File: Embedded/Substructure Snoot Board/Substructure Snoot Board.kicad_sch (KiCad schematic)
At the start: 33 parts, among them J1 10171746-00021LF, J2 PWR Jumper Pins, J3 L0 JST, J4 L1 JST, J6 A JST, J7 S Pins A, J8 S Pins B, U1 D0 FFC, U2 D1 FFC, U3 U FFC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

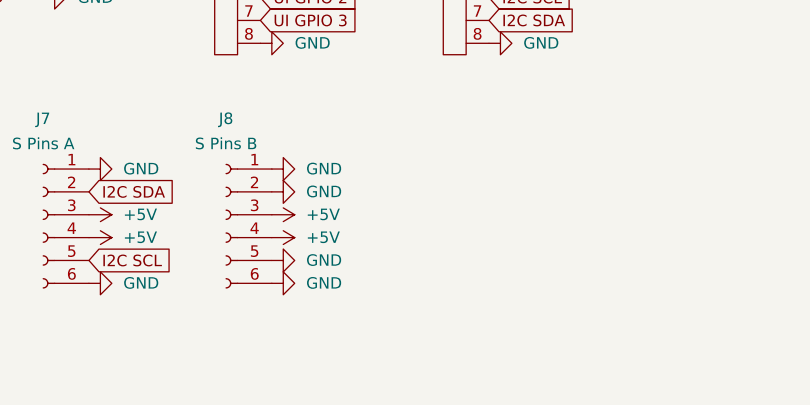
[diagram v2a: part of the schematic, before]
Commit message: Added Enable Pins to PSU Connector
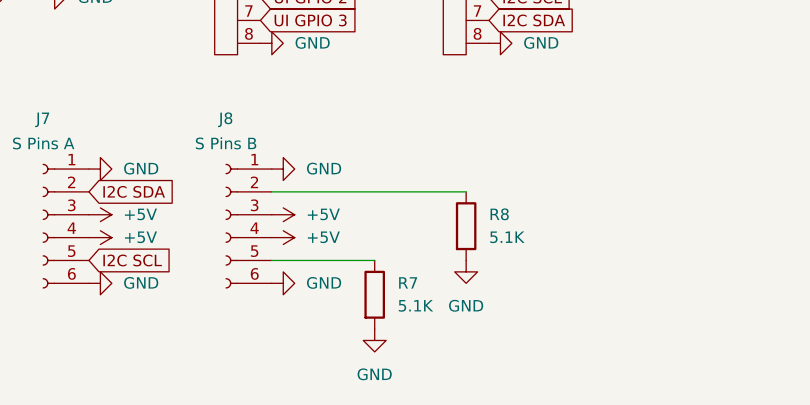
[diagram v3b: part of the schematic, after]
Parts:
- added R7, R8: 5.1K, Resistor_SMD:R_0603_1608Metric, symbol Device:R
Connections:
- net GND: now also R7.2, R8.2; no longer J8.2 (Pin_2), J8.5 (Pin_5)
- new net: J8.2 (Pin_2), R8.1
- new net: J8.5 (Pin_5), R7.1
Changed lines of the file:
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@@
 	(wire
 		(pts
+			(xy 81.28 187.96) (xy 92.71 187.96)
+		)
+		(stroke
+			(width 0)
+			(type default)
+		)
+	)
+	(wire
+		(pts
 			(xy 182.88 74.93) (xy 182.88 77.47)
 		)
@@
 	(wire
 		(pts
+			(xy 81.28 180.34) (xy 102.87 180.34)
+		)
+		(stroke
+			(width 0)
+			(type default)
+		)
+	)
+	(wire
+		(pts
 			(xy 191.77 95.25) (xy 191.77 97.79)
 		)
@@
 	)
 	(symbol
+		(lib_id "power:GND")
+		(at 92.71 195.58 0)
+		(unit 1)
+		(exclude_from_sim no)
+		(in_bom yes)
+		(on_board yes)
+		(dnp no)
+		(fields_autoplaced yes)
+		(property "Reference" "#PWR049"
+			(at 92.71 201.93 0)
+			(effects
+				(font
+					(size 1.27 1.27)
+				)
+				(hide yes)
+			)
+		)
+		(property "Value" "GND"
+			(at 92.71 200.66 0)
+			(effects
+				(font
+					(size 1.27 1.27)
+				)
+			)
+		)
+		(property "Footprint" ""
+			(at 92.71 195.58 0)
+			(effects
+				(font
+					(size 1.27 1.27)
+				)
+				(hide yes)
+			)
+		)
+		(property "Datasheet" ""
+			(at 92.71 195.58 0)
+			(effects
+				(font
+					(size 1.27 1.27)
+				)
+				(hide yes)
+			)
+		)
+		(property "Description" "Power symbol creates a global label with name \"GND\" , ground"
+			(at 92.71 195.58 0)
+			(effects
+				(font
+					(size 1.27 1.27)
+				)
+				(hide yes)
+			)
+		)
+		(pin "1"
+		)
+		(instances
+			(project "Substructure Snoot Board"
+				(path "/f2fe47b0-47e9-4c85-8000-2f6998edcf1c"
+					(reference "#PWR049")
+					(unit 1)
+				)
+			)
+		)
+	)
+	(symbol
 		(lib_id "FFC:FFC-20")
 		(at 50.8 88.9 0)
@@
 	)
 	(symbol
+		(lib_id "Device:R")
+		(at 102.87 184.15 0)
+		(unit 1)
+		(exclude_from_sim no)
+		(in_bom yes)
+		(on_board yes)
+		(dnp no)
+		(property "Reference" "R8"
+			(at 105.41 182.8799 0)
+			(effects
+				(font
+					(size 1.27 1.27)
+				)
+				(justify left)
+			)
+		)
+		(property "Value" "5.1K"
+			(at 105.41 185.4199 0)
+			(effects
+				(font
+					(size 1.27 1.27)
+				)
+				(justify left)
+			)
+		)
+		(property "Footprint" "Resistor_SMD:R_0603_1608Metric"
+			(at 101.092 184.15 90)
+			(effects
+				(font
+					(size 1.27 1.27)
+				)
+				(hide yes)
+			)
+		)
+		(property "Datasheet" "~"
+			(at 102.87 184.15 0)
+			(effects
+				(font
+					(size 1.27 1.27)
+				)
+				(hide yes)
+			)
+		)
+		(property "Description" "Resistor"
+			(at 102.87 184.15 0)
+			(effects
+				(font
+					(size 1.27 1.27)
+				)
+				(hide yes)
+			)
+		)
+		(pin "2"
+		)
+		(pin "1"
+		)
+		(instances
+			(project "Substructure Snoot Board"
+				(path "/f2fe47b0-47e9-4c85-8000-2f6998edcf1c"
+					(reference "R8")
+					(unit 1)
+				)
+			)
+		)
+	)
+	(symbol
 		(lib_id "FFC:FFC-8")
 		(at 101.6 154.94 0)
@@
 	)
 	(symbol
-		(lib_id "power:GND")
-		(at 29.21 146.05 90)
+		(lib_id "Device:R")
+		(at 92.71 191.77 0)
 		(unit 1)
 		(exclude_from_sim no)
@@
 		(on_board yes)
 		(dnp no)
-		(fields_autoplaced yes)
-		(property "Reference" "#PWR021"
-			(at 35.56 146.05 0)
+		(property "Reference" "R7"
+			(at 95.25 190.4999 0)
 			(effects
 				(font
 					(size 1.27 1.27)
 				)
-				(hide yes)
+				(justify left)
 			)
 		)
-		(property "Value" "GND"
-			(at 33.02 146.0499 90)
+		(property "Value" "5.1K"
+			(at 95.25 193.0399 0)
 			(effects
 				(font
 					(size 1.27 1.27)
 				)
-				(justify right)
+				(justify left)
 			)
 		)
-		(property "Footprint" ""
-			(at 29.21 146.05 0)
+		(property "Footprint" "Resistor_SMD:R_0603_1608Metric"
+			(at 90.932 191.77 90)
 			(effects
 				(font
@@
 			)
 		)
-		(property "Datasheet" ""
-			(at 29.21 146.05 0)
+		(property "Datasheet" "~"
+			(at 92.71 191.77 0)
 			(effects
 				(font
@@
 			)
 		)
-		(property "Description" "Power symbol creates a global label with name \"GND\" , ground"
-			(at 29.21 146.05 0)
+		(property "Description" "Resistor"
+			(at 92.71 191.77 0)
 			(effects
 				(font
@@
 		(pin "1"
 		)
+		(pin "2"
+		)
 		(instances
 			(project "Substructure Snoot Board"
 				(path "/f2fe47b0-47e9-4c85-8000-2f6998edcf1c"
-					(reference "#PWR021")
+					(reference "R7")
 					(unit 1)
 				)
@@
 	)
 	(symbol
-		(lib_id "power:+3V3")
-		(at 134.62 87.63 0)
+		(lib_id "power:GND")
+		(at 29.21 146.05 90)
 		(unit 1)
 		(exclude_from_sim no)
@@
 		(dnp no)
 		(fields_autoplaced yes)
-		(property "Reference" "#PWR031"
-			(at 134.62 91.44 0)
+		(property "Reference" "#PWR021"
+			(at 35.56 146.05 0)
 			(effects
 				(font
@@
 			)
 		)
-		(property "Value" "+3V3"
-			(at 134.62 82.55 0)
+		(property "Value" "GND"
+			(at 33.02 146.0499 90)
 			(effects
 				(font
 					(size 1.27 1.27)
 				)
+				(justify right)
 			)
 		)
 		(property "Footprint" ""
-			(at 134.62 87.63 0)
+			(at 29.21 146.05 0)
 			(effects
 				(font
@@
 		)
 		(property "Datasheet" ""
-			(at 134.62 87.63 0)
+			(at 29.21 146.05 0)
 			(effects
 				(font
@@
 			)
 		)
-		(property "Description" "Power symbol creates a global label with name \"+3V3\""
-			(at 134.62 87.63 0)
+		(property "Description" "Power symbol creates a global label with name \"GND\" , ground"
+			(at 29.21 146.05 0)
 			(effects
 				(font
@@
 			(project "Substructure Snoot Board"
 				(path "/f2fe47b0-47e9-4c85-8000-2f6998edcf1c"
-					(reference "#PWR031")
+					(reference "#PWR021")
 					(unit 1)
 				)
@@
 	)
 	(symbol
-		(lib_id "power:GND")
-		(at 81.28 187.96 90)
+		(lib_id "power:+3V3")
+		(at 134.62 87.63 0)
 		(unit 1)
 		(exclude_from_sim no)
@@
 		(dnp no)
 		(fields_autoplaced yes)
-		(property "Reference" "#PWR080"
-			(at 87.63 187.96 0)
+		(property "Reference" "#PWR031"
+			(at 134.62 91.44 0)
 			(effects
 				(font
@@
 			)
 		)
-		(property "Value" "GND"
-			(at 85.09 187.9599 90)
+		(property "Value" "+3V3"
+			(at 134.62 82.55 0)
 			(effects
 				(font
 					(size 1.27 1.27)
 				)
-				(justify right)
 			)
 		)
 		(property "Footprint" ""
-			(at 81.28 187.96 0)
+			(at 134.62 87.63 0)
 			(effects
 				(font
@@
 		)
 		(property "Datasheet" ""
-			(at 81.28 187.96 0)
+			(at 134.62 87.63 0)
 			(effects
 				(font
@@
 			)
 		)
-		(property "Description" "Power symbol creates a global label with name \"GND\" , ground"
-			(at 81.28 187.96 0)
+		(property "Description" "Power symbol creates a global label with name \"+3V3\""
+			(at 134.62 87.63 0)
 			(effects
 				(font
@@
 			(project "Substructure Snoot Board"
 				(path "/f2fe47b0-47e9-4c85-8000-2f6998edcf1c"
-					(reference "#PWR080")
+					(reference "#PWR031")
 					(unit 1)
 				)
@@
 	(symbol
 		(lib_id "power:GND")
-		(at 81.28 180.34 90)
+		(at 102.87 187.96 0)
 		(unit 1)
 		(exclude_from_sim no)
@@
 		(dnp no)
 		(fields_autoplaced yes)
-		(property "Reference" "#PWR079"
-			(at 87.63 180.34 0)
+		(property "Reference" "#PWR050"
+			(at 102.87 194.31 0)
 			(effects
 				(font
@@
 		)
 		(property "Value" "GND"
-			(at 85.09 180.3399 90)
+			(at 102.87 193.04 0)
 			(effects
 				(font
 					(size 1.27 1.27)
 				)
-				(justify right)
 			)
 		)
 		(property "Footprint" ""
-			(at 81.28 180.34 0)
+			(at 102.87 187.96 0)
 			(effects
 				(font
@@
 		)
 		(property "Datasheet" ""
-			(at 81.28 180.34 0)
+			(at 102.87 187.96 0)
 			(effects
 				(font
@@
 		)
 		(property "Description" "Power symbol creates a global label with name \"GND\" , ground"
-			(at 81.28 180.34 0)
+			(at 102.87 187.96 0)
 			(effects
 				(font
@@
 			(project "Substructure Snoot Board"
 				(path "/f2fe47b0-47e9-4c85-8000-2f6998edcf1c"
-					(reference "#PWR079")
+					(reference "#PWR050")
 					(unit 1)
 				)

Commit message: Modified S Pins to Mill Max
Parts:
- J7, J8: footprint Connector_PinHeader_2.54mm:PinHeader_1x06_P2.54mm_Vertical -> Connector_PinSocket_2.54mm:PinSocket_1x06_P2.54mm_Vertical
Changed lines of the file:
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@@
 			)
 		)
-		(property "Footprint" "Connector_PinHeader_2.54mm:PinHeader_1x06_P2.54mm_Vertical"
+		(property "Footprint" "Connector_PinSocket_2.54mm:PinSocket_1x06_P2.54mm_Vertical"
 			(at 76.2 182.88 0)
 			(effects
@@
 			)
 		)
-		(property "Footprint" "Connector_PinHeader_2.54mm:PinHeader_1x06_P2.54mm_Vertical"
+		(property "Footprint" "Connector_PinSocket_2.54mm:PinSocket_1x06_P2.54mm_Vertical"
 			(at 55.88 182.88 0)
 			(effects

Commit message: Added Extra Power Pads to the Bottom
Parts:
- added J5: 5Vout, TestPoint:TestPoint_Pad_D4.0mm, symbol Connector:Conn_01x01_Pin
- added J9: GNDout, TestPoint:TestPoint_Pad_D4.0mm, symbol Connector:Conn_01x01_Pin
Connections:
- net +5V: now also J5.1 (Pin_1)
- net GND: now also J9.1 (Pin_1)

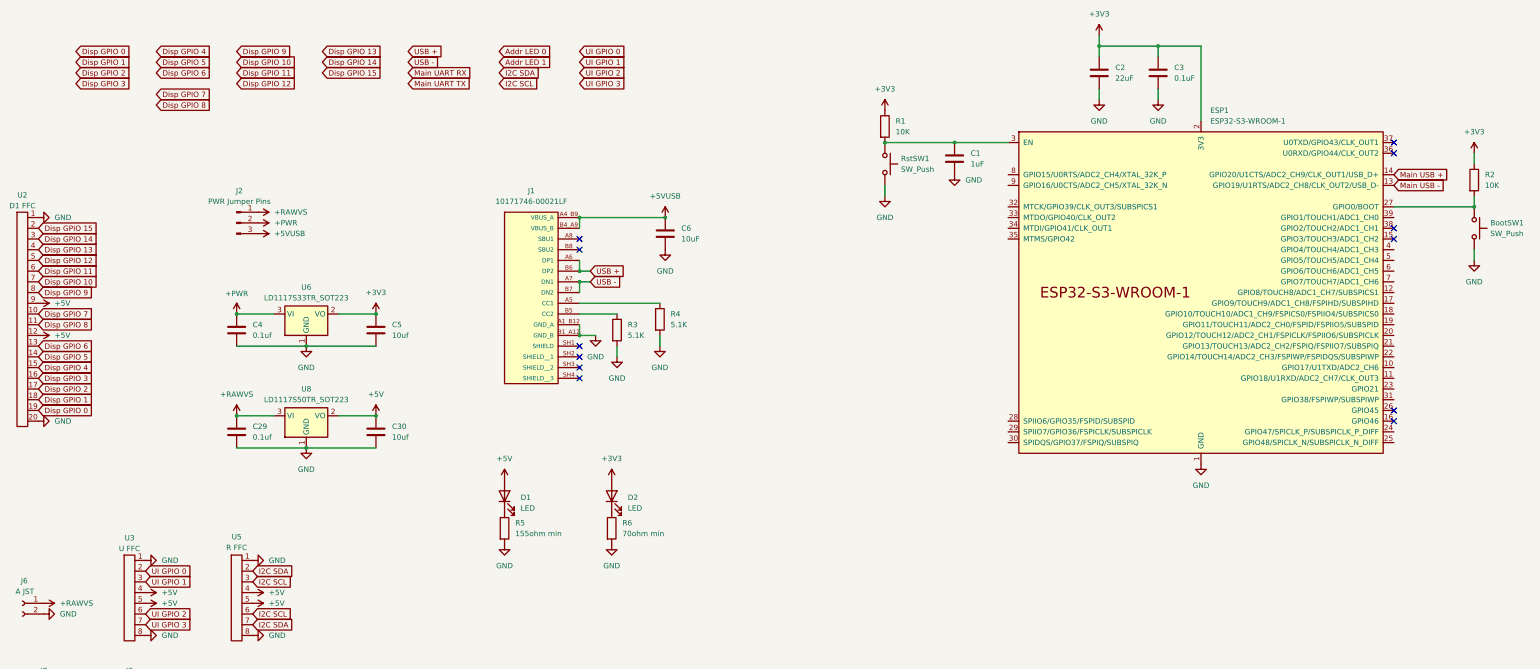
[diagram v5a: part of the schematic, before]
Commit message: Added Display Signal Routing Ideation
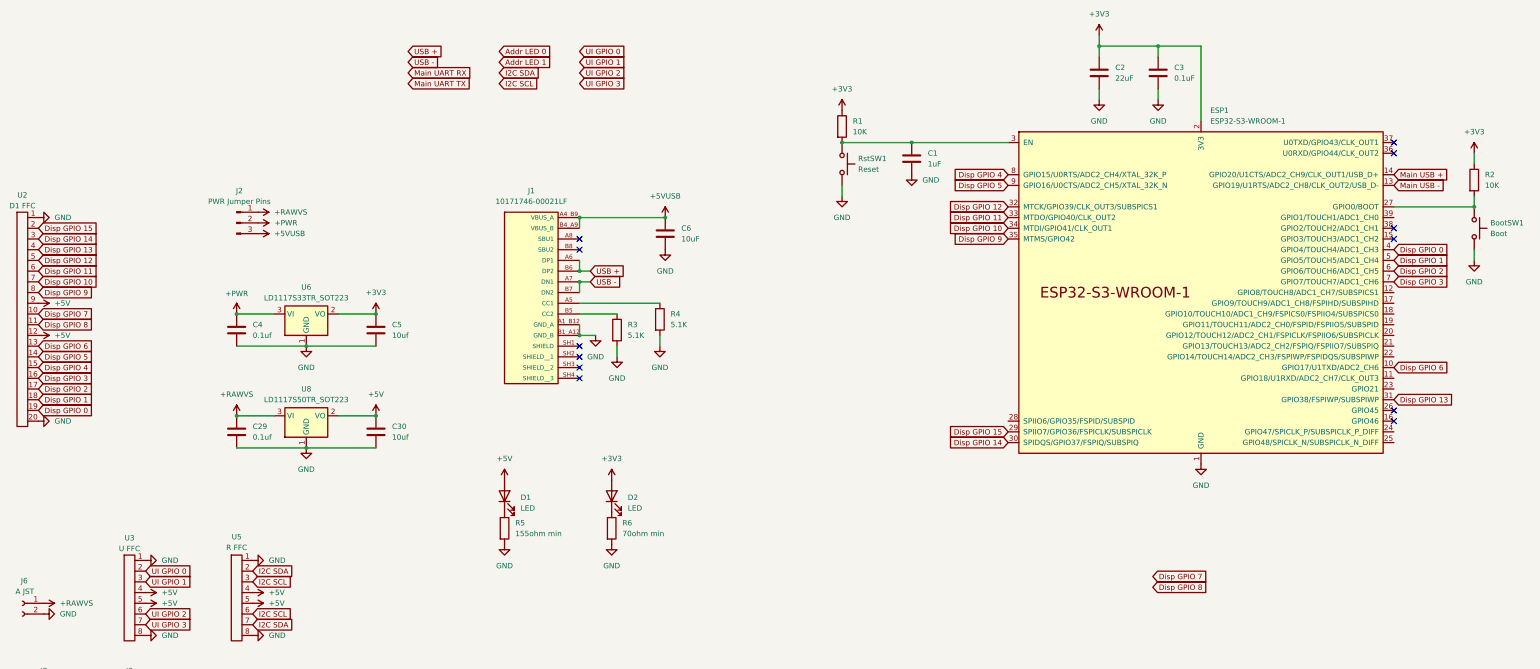
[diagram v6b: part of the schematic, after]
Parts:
- BootSW1: value SW_Push -> Boot
- RstSW1: value SW_Push -> Reset
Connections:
- net Disp GPIO 0: now also ESP1.4 (GPIO4/TOUCH4/ADC1_CH3)
- net Disp GPIO 1: now also ESP1.5 (GPIO5/TOUCH5/ADC1_CH4)
- net Disp GPIO 10: now also ESP1.34 (MTDI/GPIO41/CLK_OUT1)
- net Disp GPIO 11: now also ESP1.33 (MTDO/GPIO40/CLK_OUT2)
- net Disp GPIO 12: now also ESP1.32 (MTCK/GPIO39/CLK_OUT3/SUBSPICS1)
- net Disp GPIO 13: now also ESP1.31 (GPIO38/FSPIWP/SUBSPIWP)
- net Disp GPIO 14: now also ESP1.30 (SPIDQS/GPIO37/FSPIQ/SUBSPIQ)
- net Disp GPIO 15: now also ESP1.29 (SPIIO7/GPIO36/FSPICLK/SUBSPICLK)
- net Disp GPIO 2: now also ESP1.6 (GPIO6/TOUCH6/ADC1_CH5)
- net Disp GPIO 3: now also ESP1.7 (GPIO7/TOUCH7/ADC1_CH6)
- net Disp GPIO 4: now also ESP1.8 (GPIO15/U0RTS/ADC2_CH4/XTAL_32K_P)
- net Disp GPIO 5: now also ESP1.9 (GPIO16/U0CTS/ADC2_CH5/XTAL_32K_N)
- net Disp GPIO 6: now also ESP1.10 (GPIO17/U1TXD/ADC2_CH6)
- net Disp GPIO 9: now also ESP1.35 (MTMS/GPIO42)
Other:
- moved on the sheet: C1, R1, RstSW1

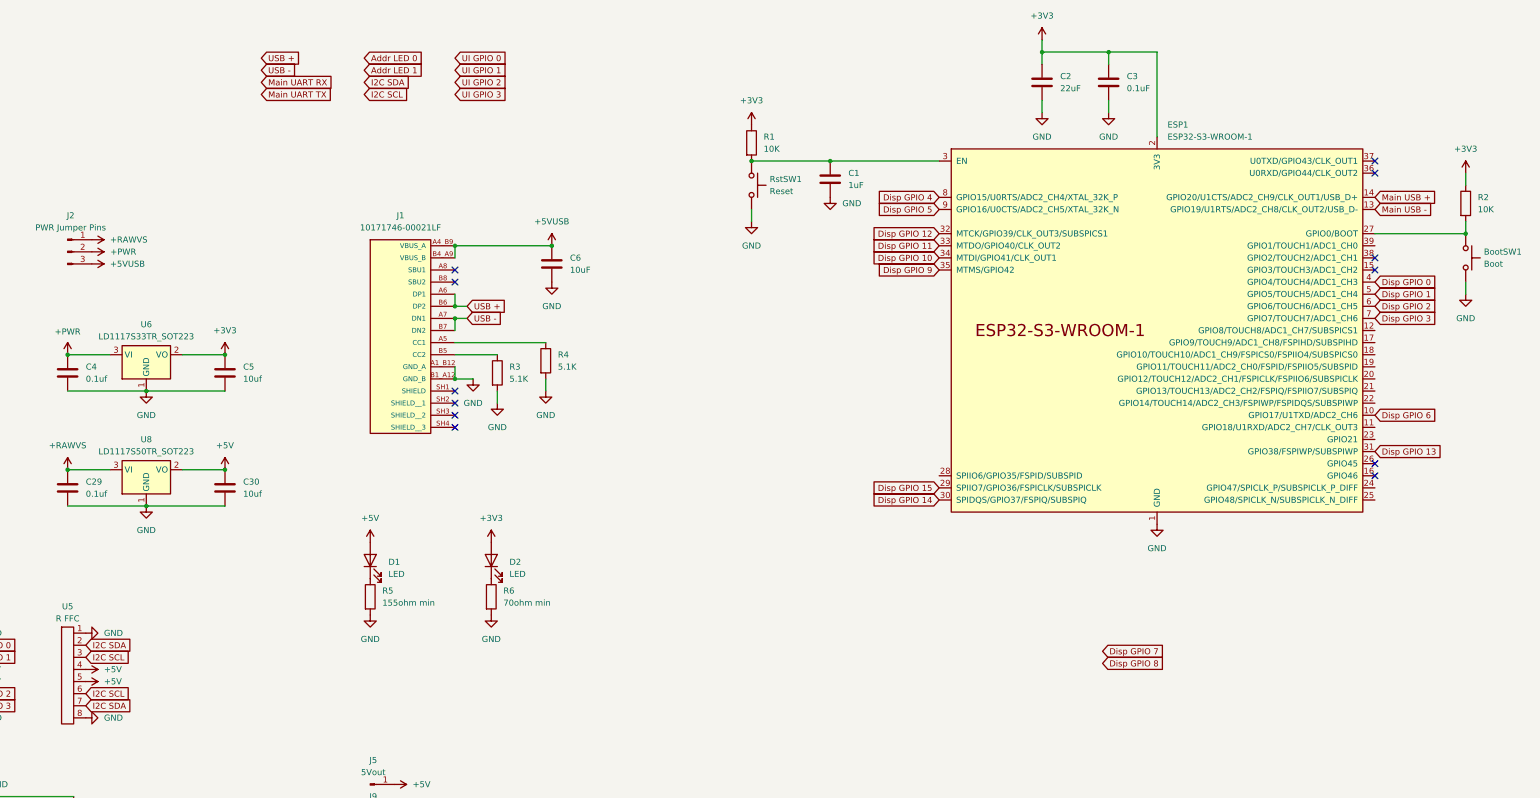
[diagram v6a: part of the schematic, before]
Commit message: Added Routing (Ideation)
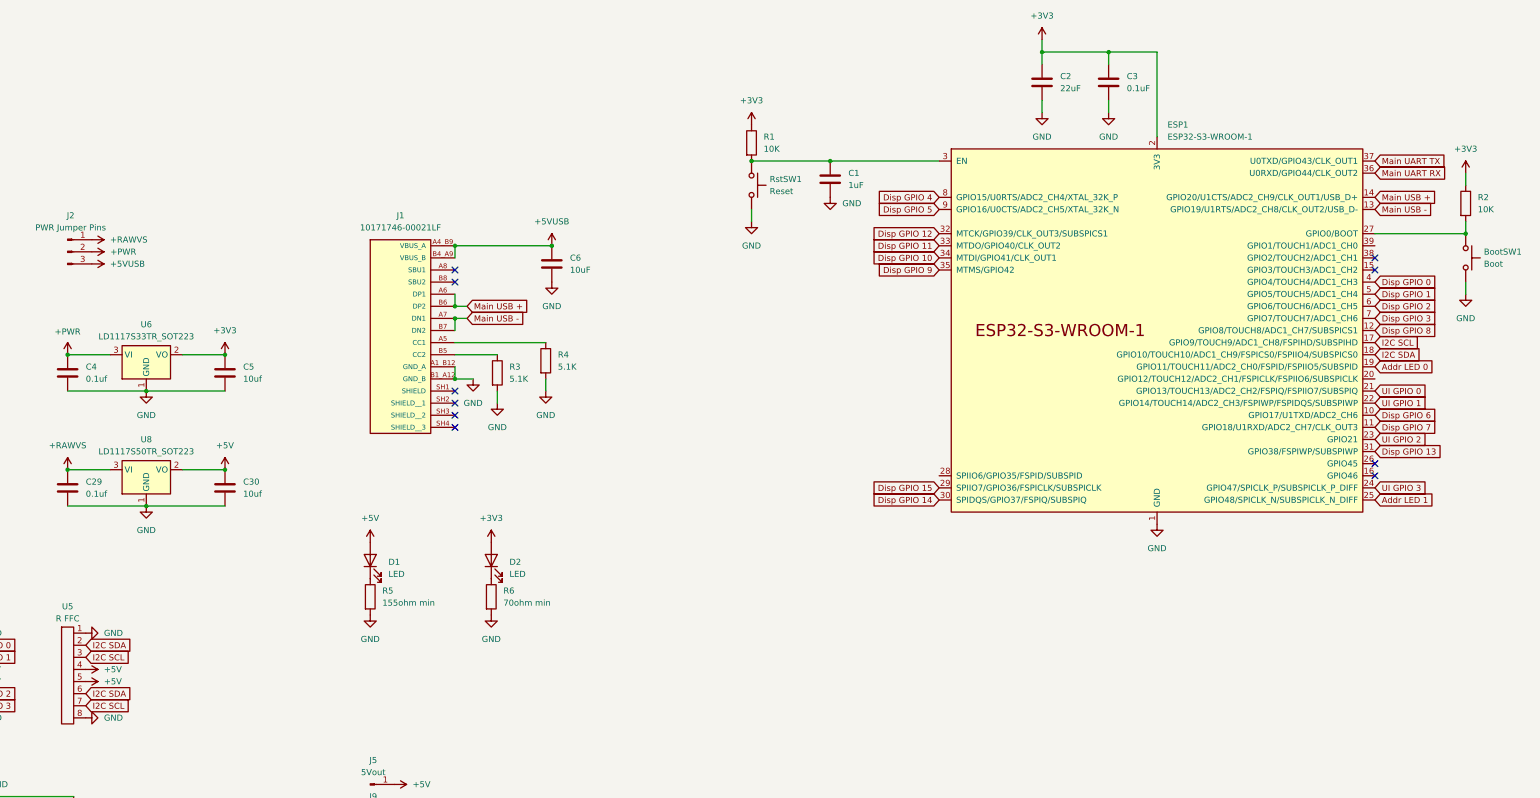
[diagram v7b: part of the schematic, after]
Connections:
- net USB + is gone; now on net Main USB +: J1.A6 (DP1), J1.B6 (DP2)
- net USB - is gone; now on net Main USB -: J1.A7 (DN1), J1.B7 (DN2)
- net Addr LED 0: now also ESP1.19 (GPIO11/TOUCH11/ADC2_CH0/FSPID/FSPIIO5/SUBSPID)
- net Addr LED 1: now also ESP1.25 (GPIO48/SPICLK_N/SUBSPICLK_N_DIFF)
- net Disp GPIO 7: now also ESP1.11 (GPIO18/U1RXD/ADC2_CH7/CLK_OUT3)
- net Disp GPIO 8: now also ESP1.12 (GPIO8/TOUCH8/ADC1_CH7/SUBSPICS1)
- net I2C SCL: now also ESP1.17 (GPIO9/TOUCH9/ADC1_CH8/FSPIHD/SUBSPIHD), U5.7; no longer U5.6
- net I2C SDA: now also ESP1.18 (GPIO10/TOUCH10/ADC1_CH9/FSPICS0/FSPIIO4/SUBSPICS0), U5.6; no longer U5.7
- net Main UART RX: now also ESP1.36 (U0RXD/GPIO44/CLK_OUT2)
- net Main UART TX: now also ESP1.37 (U0TXD/GPIO43/CLK_OUT1)
- net UI GPIO 0: now also ESP1.21 (GPIO13/TOUCH13/ADC2_CH2/FSPIQ/FSPIIO7/SUBSPIQ)
- net UI GPIO 1: now also ESP1.22 (GPIO14/TOUCH14/ADC2_CH3/FSPIWP/FSPIDQS/SUBSPIWP)
- net UI GPIO 2: now also ESP1.23 (GPIO21)
- net UI GPIO 3: now also ESP1.24 (GPIO47/SPICLK_P/SUBSPICLK_P_DIFF)
- no-connect marks 12 -> 10
